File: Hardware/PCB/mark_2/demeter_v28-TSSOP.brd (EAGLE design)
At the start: 90 x 56 mm, 69 parts, among them IC1 4050, IC2 LM1117-5.0, IC3 LM1117-3.3, IC5 MCP3424T, IC6 MCP23017SO, IC8 ATMEGA32U4-AU, Q1 IRLML6402, Q3 IRLML6402, Q5 IRLML6402

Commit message: 
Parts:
- moved JP1 0.13 mm to (45.1, 19.1)
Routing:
- net GND: track 489.6 -> 486.2 mm
- net +3V3: track 239.9 -> 237.9 mm
- net +5V: track 300.7 -> 302.4 mm
- net N$9: track 60.0 -> 61.7 mm
- net N$33: track 45.1 -> 46.6 mm
- net N$10: track 33.5 -> 34.3 mm

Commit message: 
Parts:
- R3, R6, R8: value (none) -> 10k
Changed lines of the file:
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@@
 <?xml version="1.0" encoding="utf-8"?>
 <!DOCTYPE eagle SYSTEM "eagle.dtd">
-<eagle version="6.1">
+<eagle version="6.2">
 <drawing>
 <settings>
@@
 <setting verticaltext="up"/>
 </settings>
-<grid distance="0.025" unitdist="inch" unit="mm" style="lines" multiple="2" display="yes" altdistance="0.005" altunitdist="inch" altunit="mm"/>
+<grid distance="0.05" unitdist="inch" unit="inch" style="lines" multiple="2" display="yes" altdistance="0.005" altunitdist="inch" altunit="inch"/>
 <layers>
 <layer number="1" name="Top" color="4" fill="1" visible="yes" active="yes"/>
@@
 <layer number="39" name="tKeepout" color="4" fill="11" visible="yes" active="yes"/>
 <layer number="40" name="bKeepout" color="1" fill="11" visible="yes" active="yes"/>
-<layer number="41" name="tRestrict" color="4" fill="10" visible="yes" active="yes"/>
-<layer number="42" name="bRestrict" color="1" fill="10" visible="yes" active="yes"/>
+<layer number="41" name="tRestrict" color="4" fill="10" visible="no" active="yes"/>
+<layer number="42" name="bRestrict" color="1" fill="10" visible="no" active="yes"/>
 <layer number="43" name="vRestrict" color="2" fill="10" visible="no" active="yes"/>
 <layer number="44" name="Drills" color="7" fill="1" visible="no" active="yes"/>
@@
 <element name="JK1" library="mark_2" package="AUDIO-JACK" value="" x="86.36" y="13.97" rot="R180"/>
 <element name="R4" library="mark_2" package="R0805" value="" x="78.105" y="16.51" rot="MR180"/>
-<element name="R8" library="mark_2" package="R0805" value="" x="58.42" y="27.94" rot="R180"/>
+<element name="R8" library="mark_2" package="R0805" value="10k" x="58.42" y="27.94" rot="R180"/>
 <element name="D2" library="mark_2" package="SOD123" value="" x="70.485" y="11.43" rot="MR270"/>
 <element name="Q2" library="mark_2" package="SOT23" value="" x="73.66" y="17.78" rot="MR90"/>
@@
 <element name="Q5" library="mark_2" package="SOT23" value="IRLML6402" x="73.66" y="39.37" rot="MR90"/>
 <element name="JK3" library="mark_2" package="AUDIO-JACK" value="" x="86.36" y="41.91" rot="R180"/>
-<element name="R6" library="mark_2" package="R0805" value="" x="78.105" y="44.45" rot="MR180"/>
+<element name="R6" library="mark_2" package="R0805" value="10k" x="78.105" y="44.45" rot="MR180"/>
 <element name="D6" library="mark_2" package="SOD123" value="" x="70.485" y="39.37" rot="MR270"/>
 <element name="Q6" library="mark_2" package="SOT23" value="" x="73.66" y="45.72" rot="MR90"/>
@@
 <element name="IC8" library="mark_2" package="TQFP44" value="ATMEGA32U4-AU" x="45.085" y="33.147" rot="MR45"/>
 <element name="JP1" library="mark_2" package="AVR-ISP-6" value="AVR-ISP-6" x="45.085" y="19.05"/>
-<element name="R3" library="mark_2" package="R0805" value="" x="40.005" y="19.05" rot="MR90"/>
+<element name="R3" library="mark_2" package="R0805" value="10k" x="40.005" y="19.05" rot="MR90"/>
 <element name="C1" library="mark_2" package="C0805K" value="1uF" x="51.308" y="25.781" rot="MR135"/>
 <element name="C8" library="mark_2" package="C0805K" value="100nF" x="50.8" y="39.37" rot="MR45"/>

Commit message: 
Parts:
- R1, R11, R12, R14, R16, R17, R19, R21, R22, R7: value (none) -> 1k
- R13, R15, R18: value (none) -> 1k5
- R4, R5: value (none) -> 10k
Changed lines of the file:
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@@
 <layers>
 <layer number="1" name="Top" color="4" fill="1" visible="yes" active="yes"/>
-<layer number="16" name="Bottom" color="1" fill="1" visible="yes" active="yes"/>
+<layer number="16" name="Bottom" color="1" fill="1" visible="no" active="yes"/>
 <layer number="17" name="Pads" color="2" fill="1" visible="yes" active="yes"/>
 <layer number="18" name="Vias" color="2" fill="1" visible="yes" active="yes"/>
@@
 <attribute name="VALUE" x="1.27" y="22.86" size="1.27" layer="27" rot="R270"/>
 </element>
-<element name="R1" library="mark_2" package="R0805" value="" x="6.35" y="21.59" rot="R270"/>
+<element name="R1" library="mark_2" package="R0805" value="1k" x="6.35" y="21.59" rot="R270"/>
 <element name="U$1" library="mark_2" package="XBEE-1" value="XBEE-1B1" x="21.59" y="25.4" rot="R180"/>
 <element name="C2" library="mark_2" package="PANASONIC_D" value="22uF" x="21.59" y="35.56" rot="R90"/>
@@
 </element>
 <element name="JK1" library="mark_2" package="AUDIO-JACK" value="" x="86.36" y="13.97" rot="R180"/>
-<element name="R4" library="mark_2" package="R0805" value="" x="78.105" y="16.51" rot="MR180"/>
+<element name="R4" library="mark_2" package="R0805" value="10k" x="78.105" y="16.51" rot="MR180"/>
 <element name="R8" library="mark_2" package="R0805" value="10k" x="58.42" y="27.94" rot="R180"/>
 <element name="D2" library="mark_2" package="SOD123" value="" x="70.485" y="11.43" rot="MR270"/>
@@
 <element name="Q3" library="mark_2" package="SOT23" value="IRLML6402" x="73.66" y="25.4" rot="MR90"/>
 <element name="JK2" library="mark_2" package="AUDIO-JACK" value="" x="86.36" y="27.94" rot="R180"/>
-<element name="R5" library="mark_2" package="R0805" value="" x="78.105" y="30.48" rot="MR180"/>
+<element name="R5" library="mark_2" package="R0805" value="10k" x="78.105" y="30.48" rot="MR180"/>
 <element name="D4" library="mark_2" package="SOD123" value="" x="70.485" y="25.4" rot="MR270"/>
 <element name="Q4" library="mark_2" package="SOT23" value="" x="73.66" y="31.75" rot="MR90"/>
@@
 <element name="R9" library="mark_2" package="R0805" value="22" x="46.99" y="12.7" rot="R270"/>
 <element name="R10" library="mark_2" package="R0805" value="22" x="43.18" y="12.7" rot="R270"/>
-<element name="R13" library="mark_2" package="R0805" value="" x="78.105" y="11.43" rot="MR180"/>
-<element name="R14" library="mark_2" package="R0805" value="" x="78.105" y="13.97" rot="MR180"/>
-<element name="R15" library="mark_2" package="R0805" value="" x="78.105" y="25.4" rot="MR180"/>
-<element name="R16" library="mark_2" package="R0805" value="" x="78.105" y="27.94" rot="MR180"/>
-<element name="R17" library="mark_2" package="R0805" value="" x="78.105" y="41.91" rot="MR180"/>
-<element name="R18" library="mark_2" package="R0805" value="" x="78.105" y="39.37" rot="MR180"/>
+<element name="R13" library="mark_2" package="R0805" value="1k5" x="78.105" y="11.43" rot="MR180"/>
+<element name="R14" library="mark_2" package="R0805" value="1k" x="78.105" y="13.97" rot="MR180"/>
+<element name="R15" library="mark_2" package="R0805" value="1k5" x="78.105" y="25.4" rot="MR180"/>
+<element name="R16" library="mark_2" package="R0805" value="1k" x="78.105" y="27.94" rot="MR180"/>
+<element name="R17" library="mark_2" package="R0805" value="1k" x="78.105" y="41.91" rot="MR180"/>
+<element name="R18" library="mark_2" package="R0805" value="1k5" x="78.105" y="39.37" rot="MR180"/>
 <element name="X2" library="mark_2" package="W237-102" value="" x="6.35" y="39.37" rot="R270"/>
 <element name="JP5" library="mark_2" package="1X03" value="" x="29.21" y="7.62" rot="R90"/>
 <element name="JP6" library="mark_2" package="1X02" value="" x="13.97" y="6.35" rot="R270"/>
 <element name="U$6" library="mark_2" package="DP9056_V1" value="" x="0" y="0"/>
-<element name="R7" library="mark_2" package="R0805" value="" x="6.35" y="28.575" rot="R90"/>
+<element name="R7" library="mark_2" package="R0805" value="1k" x="6.35" y="28.575" rot="R90"/>
 <element name="PWR" library="mark_2" package="CHIP-LED0805" value="" x="3.81" y="28.575" smashed="yes">
 <attribute name="NAME" x="5.08" y="27.94" size="1.27" layer="25"/>
@@
 <element name="C7" library="mark_2" package="C0805K" value="100nF" x="58.42" y="25.4" rot="R180"/>
 <element name="C11" library="mark_2" package="C0805K" value="100nF" x="19.05" y="9.779" rot="MR180"/>
-<element name="R11" library="mark_2" package="R0805" value="" x="77.47" y="13.97" rot="R270"/>
+<element name="R11" library="mark_2" package="R0805" value="1k" x="77.47" y="13.97" rot="R270"/>
 <element name="PWR1" library="mark_2" package="CHIP-LED0805" value="" x="75.565" y="13.97" rot="R180"/>
-<element name="R12" library="mark_2" package="R0805" value="" x="77.47" y="27.94" rot="R90"/>
+<element name="R12" library="mark_2" package="R0805" value="1k" x="77.47" y="27.94" rot="R90"/>
 <element name="PWR2" library="mark_2" package="CHIP-LED0805" value="" x="75.565" y="27.94"/>
 <element name="PWR3" library="mark_2" package="CHIP-LED0805" value="" x="75.565" y="41.91"/>
-<element name="R19" library="mark_2" package="R0805" value="" x="77.47" y="41.91" rot="R90"/>
+<element name="R19" library="mark_2" package="R0805" value="1k" x="77.47" y="41.91" rot="R90"/>
 <element name="R20" library="mark_2" package="R0805" value="10k" x="43.688" y="46.355" rot="MR180"/>
 <element name="JP2" library="mark_2" package="1X03" value="" x="44.958" y="49.53"/>
@@
 <attribute name="VALUE" x="1.27" y="11.43" size="1.27" layer="27" rot="R270"/>
 </element>
-<element name="R21" library="mark_2" package="R0805" value="" x="6.35" y="10.16" rot="R270"/>
+<element name="R21" library="mark_2" package="R0805" value="1k" x="6.35" y="10.16" rot="R270"/>
 <element name="RX" library="mark_2" package="CHIP-LED0805" value="" x="3.81" y="15.24"/>
-<element name="R22" library="mark_2" package="R0805" value="" x="6.35" y="15.24" rot="R90"/>
+<element name="R22" library="mark_2" package="R0805" value="1k" x="6.35" y="15.24" rot="R90"/>
 </elements>
 <signals>

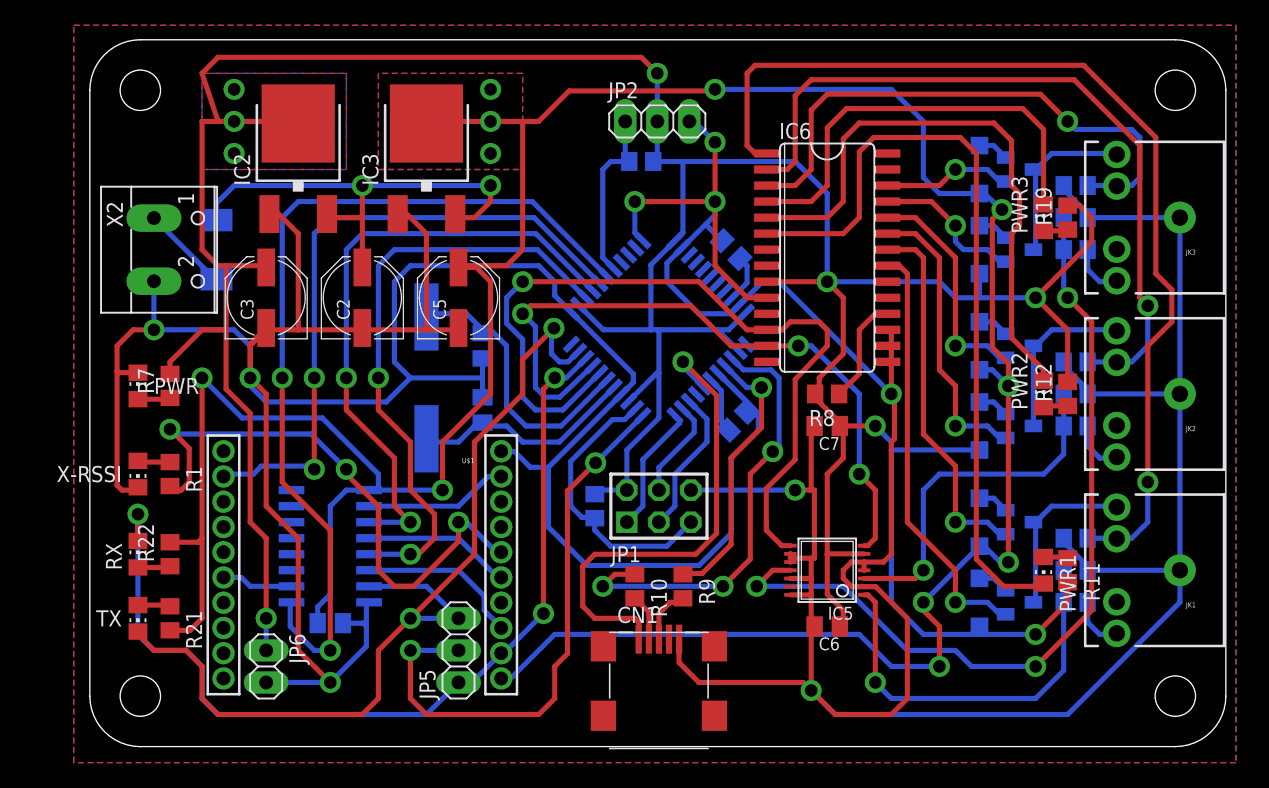
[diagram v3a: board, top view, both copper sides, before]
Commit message: 
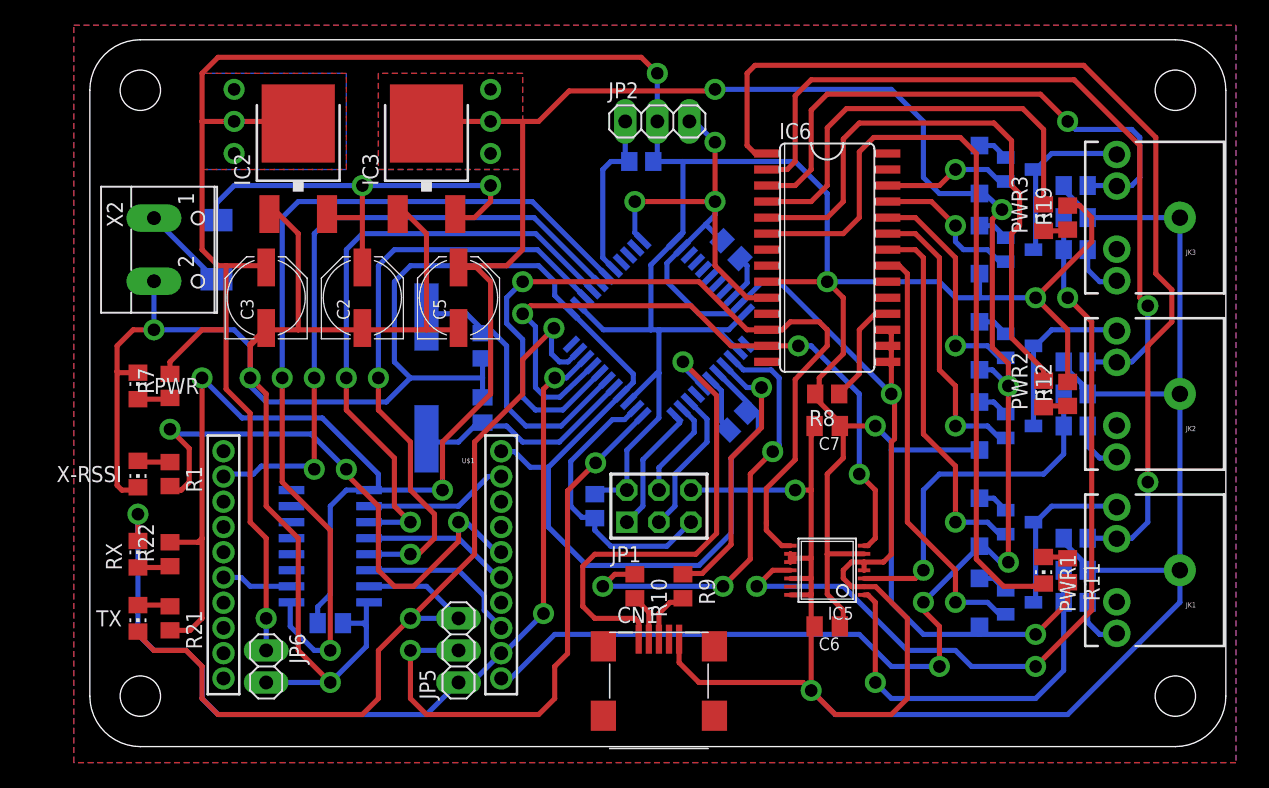
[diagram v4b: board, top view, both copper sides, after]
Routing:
- net GND: track 486.2 -> 485.7 mm
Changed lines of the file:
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@@
 <layers>
 <layer number="1" name="Top" color="4" fill="1" visible="yes" active="yes"/>
-<layer number="16" name="Bottom" color="1" fill="1" visible="no" active="yes"/>
+<layer number="16" name="Bottom" color="1" fill="1" visible="yes" active="yes"/>
 <layer number="17" name="Pads" color="2" fill="1" visible="yes" active="yes"/>
 <layer number="18" name="Vias" color="2" fill="1" visible="yes" active="yes"/>
@@
 <wire x1="63.754" y1="24.384" x2="63.5" y2="24.13" width="0.4064" layer="1"/>
 <wire x1="63.5" y1="24.13" x2="63.5" y2="15.24" width="0.4064" layer="1"/>
-<wire x1="57.15" y1="20.32" x2="57.404" y2="20.32" width="0.4064" layer="1"/>
-<wire x1="57.404" y1="20.32" x2="57.404" y2="14.9225" width="0.4064" layer="1"/>
-<wire x1="57.15" y1="14.9225" x2="57.404" y2="14.9225" width="0.4064" layer="1"/>
+<wire x1="57.15" y1="20.32" x2="57.15" y2="14.9225" width="0.4064" layer="1"/>
 </signal>
 <signal name="+3V3">
@@
 <wire x1="42.6808375" y1="27.348721875" x2="44.923115625" y2="29.591" width="0.4064" layer="16"/>
 <wire x1="44.45" y1="33.02" x2="45.085" y2="33.02" width="0.4064" layer="16"/>
-<wire x1="10.16" y1="49.53" x2="11.43" y2="49.53" width="0.4064" layer="1"/>
+<wire x1="8.89" y1="49.53" x2="11.43" y2="49.53" width="0.4064" layer="1"/>
 <wire x1="11.43" y1="49.53" x2="16.35" y2="49.53" width="0.4064" layer="1"/>
 <wire x1="8.89" y1="39.37" x2="8.89" y2="49.53" width="0.4064" layer="1"/>
@@
 <wire x1="13.83" y1="38.1" x2="13.97" y2="37.96" width="0.4064" layer="1"/>
 <wire x1="10.795" y1="28.321" x2="12.7" y2="26.416" width="0.4064" layer="1"/>
-<wire x1="8.89" y1="53.34" x2="10.16" y2="49.53" width="0.4064" layer="1"/>
+<wire x1="8.89" y1="53.34" x2="8.89" y2="49.53" width="0.4064" layer="1"/>
 <via x="13.97" y="10.16" extent="1-16" drill="1" diameter="1.6764"/>
 <wire x1="13.97" y1="10.16" x2="13.97" y2="7.62" width="0.4064" layer="16"/>
@@
 <vertex x="8.89" y="45.72"/>
 </polygon>
-<wire x1="8.89" y1="49.53" x2="10.16" y2="49.53" width="0.4064" layer="1"/>
 <polygon width="0.4064" layer="1" isolate="0.4064" thermals="no">
 <vertex x="8.89" y="53.34"/>

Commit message: 
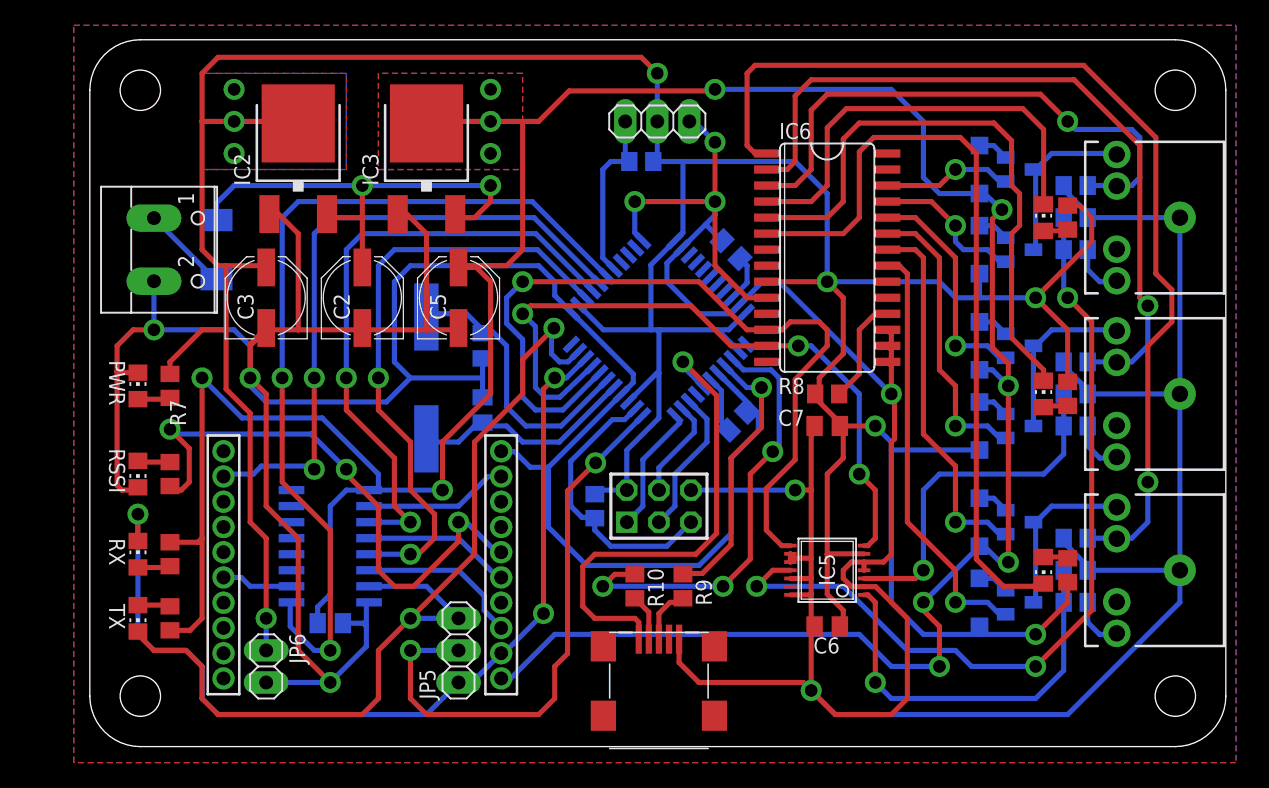
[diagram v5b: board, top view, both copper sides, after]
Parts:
- IC4: value XBEE-1B1 -> XBEE
- IC5: value MCP3424T -> MCP3424
- JP1: value AVR-ISP-6 -> AVR-ISP
- X2: value (none) -> POWER
- renumbered U$1 to IC4, X-RSSI to RSSI
